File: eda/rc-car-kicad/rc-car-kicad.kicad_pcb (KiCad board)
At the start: 2 copper layers, 88.5 x 40.5 mm, 59 parts, among them J1 Servo Sig, J10 RF 3.3V, J11 RF CE, J12 RF CSN, J13 RF SCK, J14 RF MOSI, J15 RF MISO, J16 Gnd, J17 3.3V, J19 Battery, J2 Servo Gnd, J20 8.2V, J4 DC Motor -, J5 DC Motor +, J6 ISP RESET, J9 RF Gnd, Q1 IRLML6244, Q2 IRLML2246, Q3 IRLML2246, Q4 IRLML6244, Q5 MMBT3904, Q6 MMBT3904, SW1 SW_SPST, U1 TPS3840, U3 ATmega164A-A

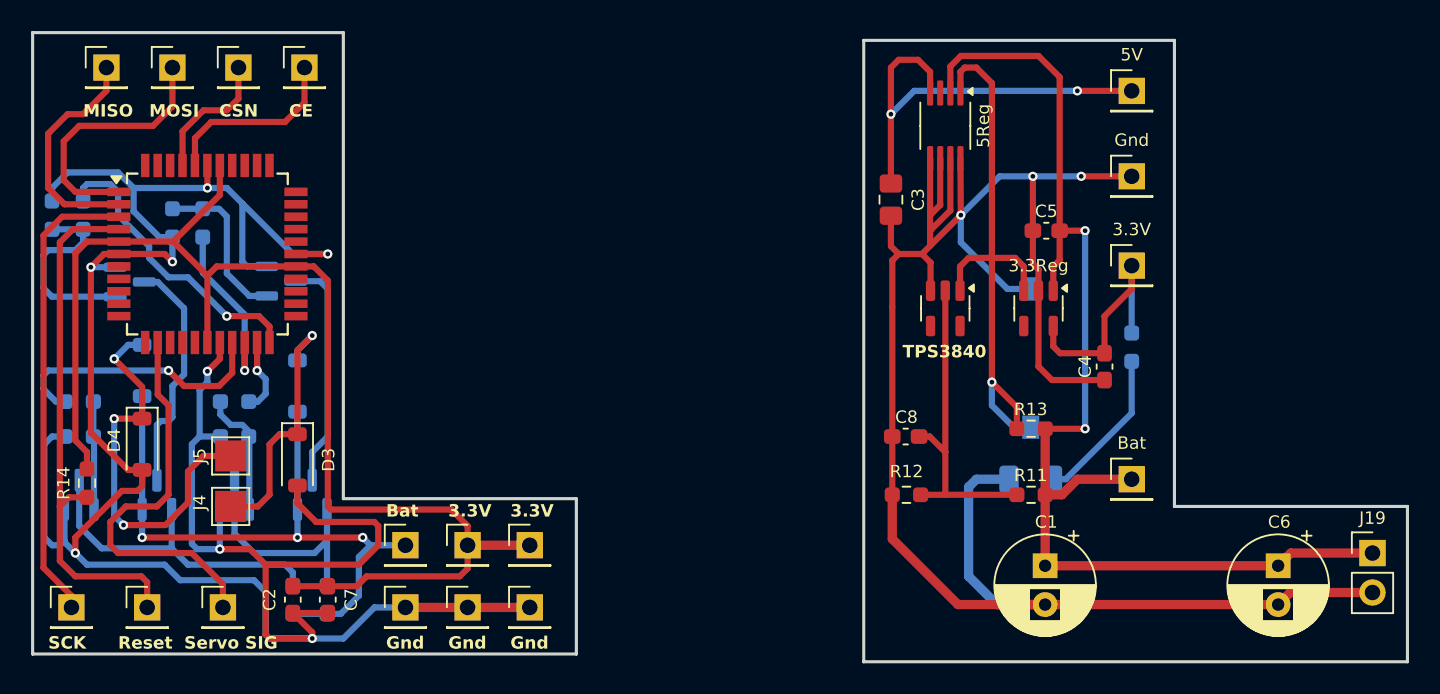
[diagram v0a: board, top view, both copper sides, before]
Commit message: - Redesigned power portion of the pcb - Changed the board to atmega164A
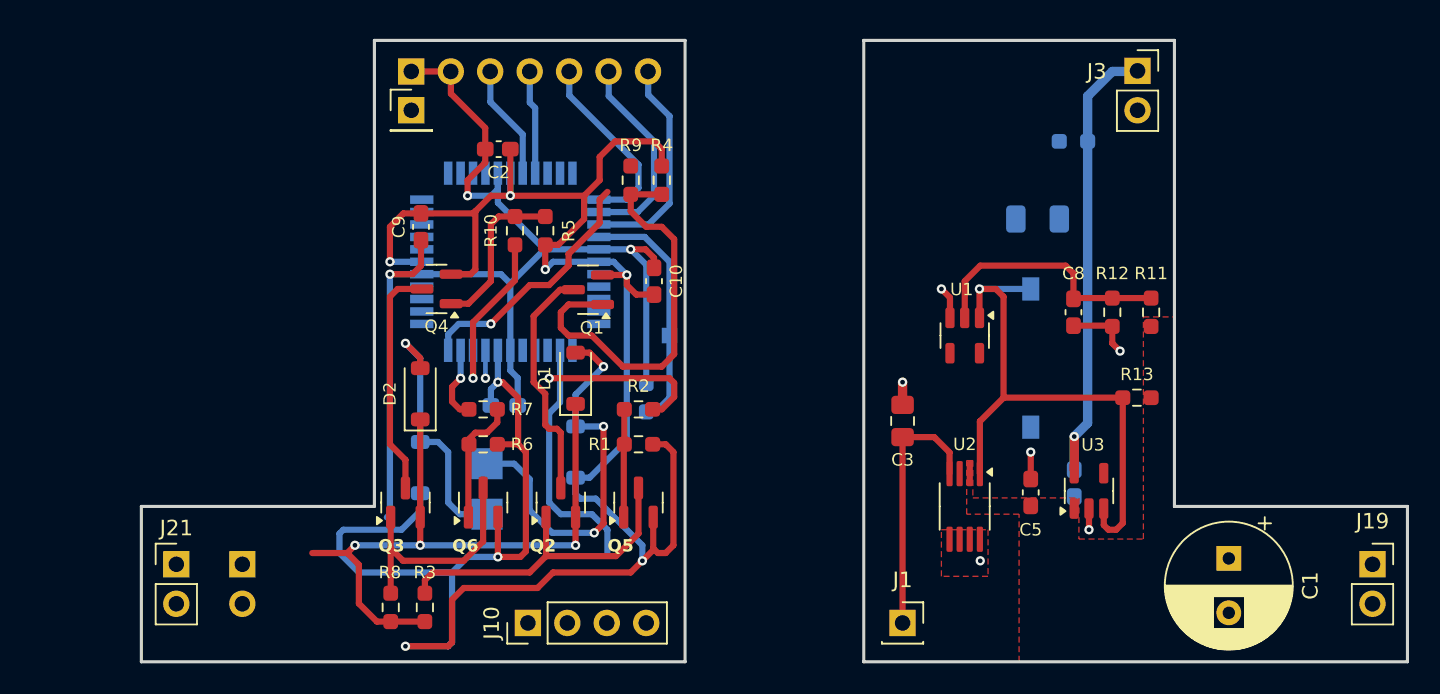
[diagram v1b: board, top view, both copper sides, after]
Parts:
- removed 3.3V, J17: 3.3V, Connector_PinHeader_2.54mm:PinHeader_1x01_P2.54mm_Vertical
- removed 5V: Servo 5V, Connector_PinHeader_2.54mm:PinHeader_1x01_P2.54mm_Vertical
- removed Bat, J20: 8.2V, Connector_PinHeader_2.54mm:PinHeader_1x01_P2.54mm_Vertical
- removed the C1 at (165.2, 134.3)
- removed Gnd: Gnd, Connector_PinHeader_2.54mm:PinHeader_1x01_P2.54mm_Vertical
- removed J12: RF CSN, Connector_PinHeader_2.54mm:PinHeader_1x01_P2.54mm_Vertical
- removed J13: RF SCK, Connector_PinHeader_2.54mm:PinHeader_1x01_P2.54mm_Vertical
- removed J14: RF MOSI, Connector_PinHeader_2.54mm:PinHeader_1x01_P2.54mm_Vertical
- removed J15: RF MISO, Connector_PinHeader_2.54mm:PinHeader_1x01_P2.54mm_Vertical
- removed J9: RF Gnd, Connector_PinHeader_2.54mm:PinHeader_1x01_P2.54mm_Vertical
- added C10: .1uF, Capacitor_SMD:C_0603_1608Metric_Pad1.08x0.95mm_HandSolder, F.Cu at (140.0, 116.0)
- added C9: .1uF, Capacitor_SMD:C_0603_1608Metric_Pad1.08x0.95mm_HandSolder, F.Cu at (125.0, 112.5)
- added J21: Battery, Connector_PinHeader_2.54mm:PinHeader_1x02_P2.54mm_Vertical, F.Cu at (109.2, 134.2)
- added J3: Battery, Connector_PinSocket_2.54mm:PinSocket_1x02_P2.54mm_Vertical, F.Cu at (171.1, 102.5)
- C1: renamed from C6; value 100uF -> 200uF; footprint Capacitor_THT:CP_Radial_D6.3mm_P2.50mm -> Capacitor_THT:CP_Radial_D8.0mm_P3.50mm
- C4, C7, D3, D4, J4, J5, R14: moved to B.Cu
- D1, D2, Q1, Q2, Q3, Q4, Q5, Q6, R1, R10, R2, R3, R4, R5, R6, R7, R8, R9: moved to F.Cu
- J1: value Servo Sig -> 5V; footprint Connector_PinHeader_2.54mm:PinHeader_1x01_P2.54mm_Vertical -> Connector_PinSocket_2.54mm:PinSocket_1x01_P2.54mm_Vertical
- J10: value RF 3.3V -> Conn_01x04; footprint Connector_PinHeader_2.54mm:PinHeader_1x01_P2.54mm_Vertical -> Connector_PinHeader_2.54mm:PinHeader_1x04_P2.54mm_Vertical
- J11: value RF CE -> Conn_01x07; footprint Connector_PinHeader_2.54mm:PinHeader_1x01_P2.54mm_Vertical -> Connector_PinHeader_2.54mm:PinHeader_1x07_P2.54mm_Vertical; moved to B.Cu
- J19: footprint Connector_PinHeader_2.54mm:PinHeader_1x02_P2.54mm_Vertical -> Connector_PinSocket_2.54mm:PinSocket_1x02_P2.54mm_Vertical
- J2: value Servo Gnd -> Battery; footprint Connector_PinHeader_2.54mm:PinHeader_1x01_P2.54mm_Vertical -> Connector_PinHeader_2.54mm:PinHeader_1x02_P2.54mm_Vertical; moved to B.Cu
- J6: footprint Connector_PinHeader_2.54mm:PinHeader_1x01_P2.54mm_Vertical -> TestPoint:TestPoint_Pad_1.0x1.0mm; moved to B.Cu
- R11: value 953k -> 470k
- R12: value 1M -> 500k
- U4: renamed from U3; moved to B.Cu
- moved J1 43.8 mm to (156.0, 138.0)
- moved R4 39.3 mm to (140.5, 109.5)
- moved J6 37.9 mm to (141.0, 119.5), turned to 180 degrees
- moved R14 36.4 mm to (139.5, 123.5)
- moved Q5 36.0 mm to (139.0, 130.2)
- moved R1 36.0 mm to (139.0, 126.5), turned to 0 degrees
- moved R2 36.0 mm to (139.0, 124.2), turned to 180 degrees
- moved R9 35.3 mm to (138.5, 109.5)
- moved J16 32.9 mm to (124.4, 105.0)
- moved C2 31.9 mm to (130.0, 107.5), turned to 0 degrees
- moved Q1 29.5 mm to (135.8, 116.5), turned to 180 degrees
- moved D1 27.9 mm to (134.9, 122.2)
- moved D4 27.9 mm to (134.9, 127.0)
- moved Q2 26.0 mm to (134.0, 130.2)
- moved U2 24.5 mm to (160.0, 130.5)
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- renumbered 5Reg to U2, 3.3Reg to U3
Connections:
- net Net-(SW1-B) renamed /U1-Reset
- net Net-(U1-VDD) renamed /U1-VDD
- C3 pad 1: +5V -> +5V Main
- J1 pad 1: /Servo Sig -> +5V Main
- J10 pad 1: +3.3V -> /Servo Sig
- J11 pad 1: /CE -> +3.3V
- J2 pad 1: GND -> +8.2V
- Q1 pad 3: Net-(Q1-D) -> Net-(D1-A)
- Q2 pad 3: Net-(Q1-D) -> Net-(D1-A)
- Q3 pad 3: Net-(Q3-D) -> Net-(D2-A)
- Q4 pad 3: Net-(Q3-D) -> Net-(D2-A)
- U2 pad 4: +5V -> +5V Main
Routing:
- net GND Main: track 130.9 -> 11.0 mm, vias 3 -> 6
- net +8.2V Main: track 76.7 -> 0.00 mm, vias 2 -> 0
- net +5V: track 28.0 -> 0.00 mm, vias 2 -> 0
- net /RESET: track 34.5 -> 15.8 mm
- net +3.3V Main: track 15.5 -> 32.8 mm, vias 0 -> 1
- net +5V Main: track 0.00 -> 16.8 mm
- net /SCK: track 30.0 -> 14.2 mm
- net Net-(D1-A): track 25.6 -> 40.9 mm
- net Net-(Q1-D): track 15.3 -> 0.00 mm
- net Net-(Q3-D): track 15.0 -> 0.00 mm
- net Net-(D2-A): track 16.9 -> 31.9 mm
- net Net-(Q1-G): track 12.7 -> 26.6 mm
- net Net-(D5-A): track 10.2 -> 0.00 mm
- net /Servo Sig: track 25.9 -> 16.1 mm
- net GND: track 163.5 -> 154.9 mm
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- added copper zone on F.Cu, net +8.2V Main
- added copper zone on B.Cu, net GND Main
- added copper zone on F.Cu, net GND Main
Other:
- board size 88.5 x 40.5 mm -> 81.5 x 40 mm
- board text added: "U1"
- board text added: "U3"
- board text removed: "Bat"
- board text removed: "Gnd"
- board text removed: "Reset"
- board text removed: "Servo SIG"
- board text removed: "TPS3840"

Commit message: - Made improvements to power and ground plains on the powere pcb - Updated the component labels in the schematic
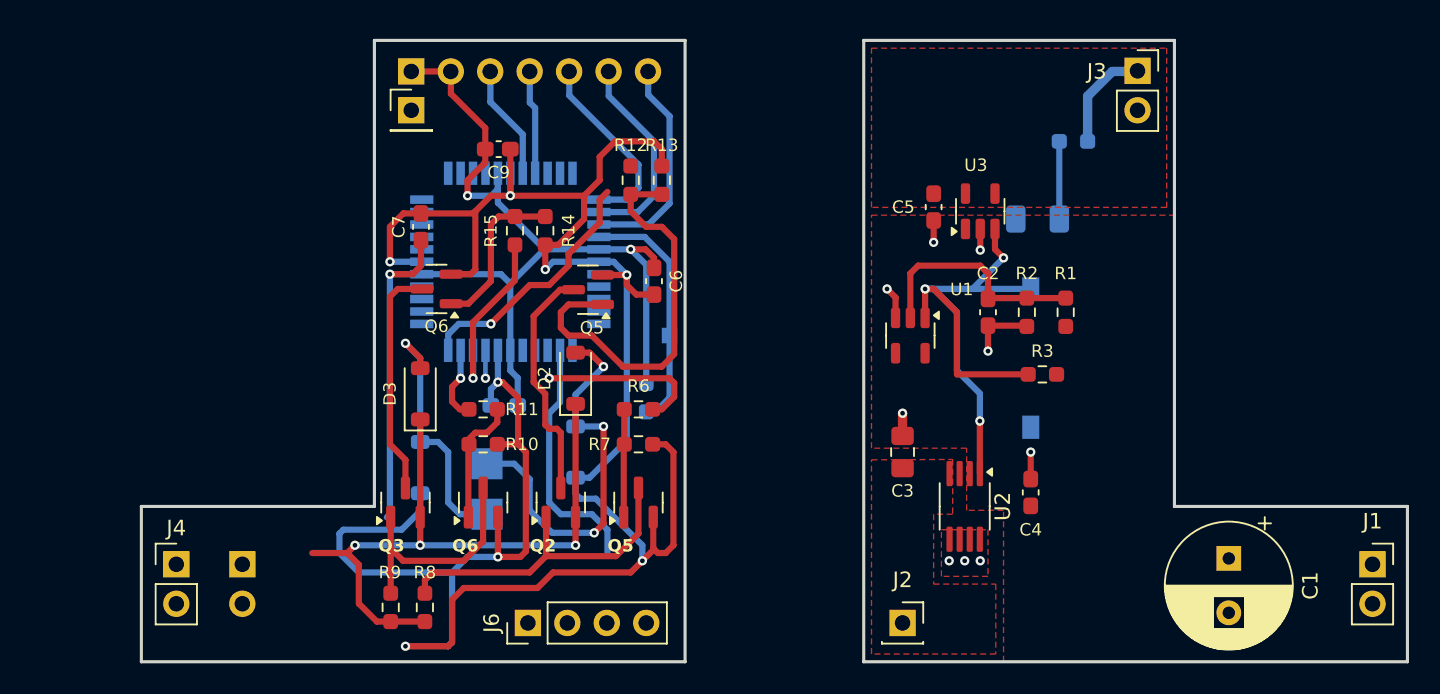
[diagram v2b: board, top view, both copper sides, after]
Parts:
- C5: renamed from C4; moved to F.Cu
- J1: renamed from J19; value Battery -> ~
- J10: renamed from J4; value DC Motor - -> ~
- J11: renamed from J6; value ISP RESET -> ~
- J2: renamed from J1; value 5V -> ~
- J3: value Battery -> ~
- J4: renamed from J21; value Battery -> ~
- J5: renamed from J2; value Battery -> ~
- J6: renamed from J10; value Conn_01x04 -> ~
- J7: renamed from J16; value Gnd -> ~
- J8: renamed from J11; value Conn_01x07 -> ~
- J9: renamed from J5; value DC Motor + -> ~
- moved C5 19.9 mm to (158.0, 111.2)
- moved U3 19.3 mm to (161.0, 111.5)
- moved R3 6.27 mm to (165.0, 122.0)
- moved C2 5.50 mm to (161.5, 118.0)
- moved R1 5.50 mm to (166.5, 118.0)
- moved R2 5.50 mm to (164.0, 118.0)
- moved U1 3.50 mm to (156.5, 119.5)
- moved C3 2.00 mm to (156.0, 127.0)
- renumbered C8 to C2, C5 to C4, C10 to C6, C9 to C7, C7 to C8, C2 to C9, D5 to D1, D1 to D2, D2 to D3, D3 to D5, Q5 to Q1, Q6 to Q4, Q1 to Q5, Q4 to Q6, R11 to R1, R6 to R10, R7 to R11, R9 to R12, R4 to R13, R5 to R14, R10 to R15, R12 to R2, R13 to R3, R15 to R4, R14 to R5, R2 to R6, R1 to R7, R3 to R8, R8 to R9
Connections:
- D1 pad 2: Net-(D5-A) -> Net-(D1-A)
- R4 pad 1: +3.3V Main -> Net-(D1-A)
- R4 pad 2: Net-(D5-A) -> +3.3V Main
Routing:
- net +3.3V Main: track 32.8 -> 6.78 mm, vias 1 -> 0
- net +5V Main: track 16.8 -> 0.00 mm
- net (no net): track 0.00 -> 5.00 mm
- net /U1-Reset: track 37.3 -> 41.6 mm, vias 1 -> 3
- net /U1-VDD: track 16.6 -> 14.9 mm
- net GND Main: track 11.0 -> 12.1 mm, vias 6 -> 9
- added copper zone on F.Cu, net +3.3V Main
- added copper zone on F.Cu, net +5V Main

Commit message: - Updated the microcontroller pcb
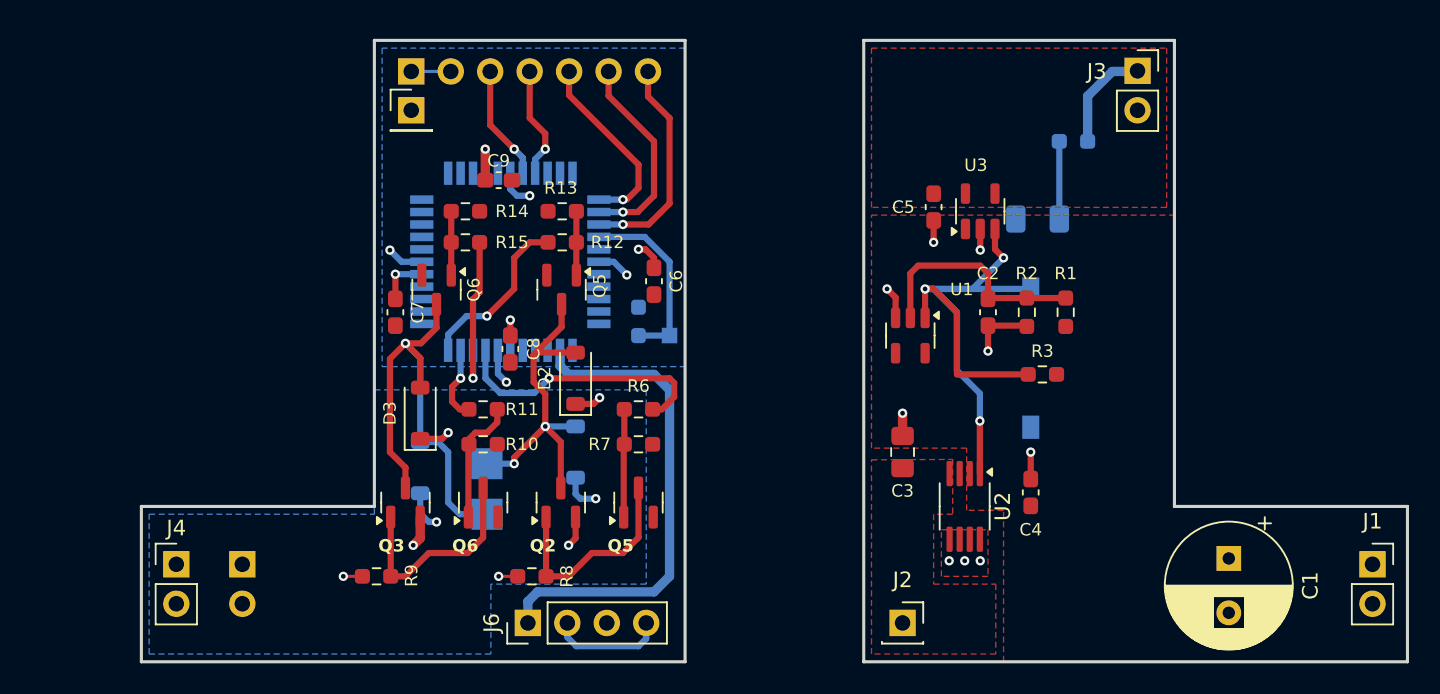
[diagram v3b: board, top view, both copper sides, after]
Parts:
- C8: moved to F.Cu
- moved R8 7.17 mm to (132.1, 135.0), turned to 0 degrees
- moved R13 6.71 mm to (134.1, 111.5), turned to 180 degrees
- moved R12 5.95 mm to (134.1, 113.5), turned to 0 degrees
- moved C7 5.74 mm to (123.3, 118.0), turned to -90 degrees
- moved R14 5.29 mm to (127.9, 111.5), turned to 0 degrees
- moved R5 4.94 mm to (139.0, 118.6)
- moved C8 3.66 mm to (130.8, 120.4), turned to -90 degrees
- moved R15 3.28 mm to (127.9, 113.5), turned to 0 degrees
- moved R9 2.20 mm to (122.1, 135.0), turned to 0 degrees
- moved C9 2.00 mm to (130.0, 109.5)
- moved Q5 1.70 mm to (134.1, 116.5), turned to -90 degrees
- moved D3 1.25 mm to (125.0, 124.5)
- turned Q6 to -90 degrees
- turned R4 to 0 degrees
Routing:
- net GND: track 154.9 -> 14.3 mm, vias 8 -> 6
- net +3.3V: track 76.9 -> 10.7 mm, vias 3 -> 4
- net +8.2V: track 42.6 -> 10.1 mm, vias 3 -> 6
- net Net-(Q5-G): track 26.6 -> 4.11 mm
- net Net-(D2-A): track 40.9 -> 23.0 mm, vias 3 -> 2
- net /Servo Sig: track 16.1 -> 31.9 mm
- net /Servo 5V: track 0.00 -> 7.45 mm
- net Net-(Q1-C): track 21.3 -> 14.0 mm
- net Net-(Q6-G): track 10.5 -> 4.11 mm
- net /Reverse_PWM: track 16.4 -> 11.1 mm
- net Net-(D1-A): track 0.00 -> 5.00 mm
- net (no net): track 5.00 -> 0.00 mm
- net /Forward_Latch: track 12.6 -> 17.5 mm, vias 2 -> 1
- net /RESET: track 15.8 -> 12.0 mm
- net Net-(Q3-G): track 15.1 -> 14.0 mm
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- added copper zone on B.Cu, net +3.3V
- added copper zone on B.Cu, net +8.2V
- added copper zone on F.Cu, net GND

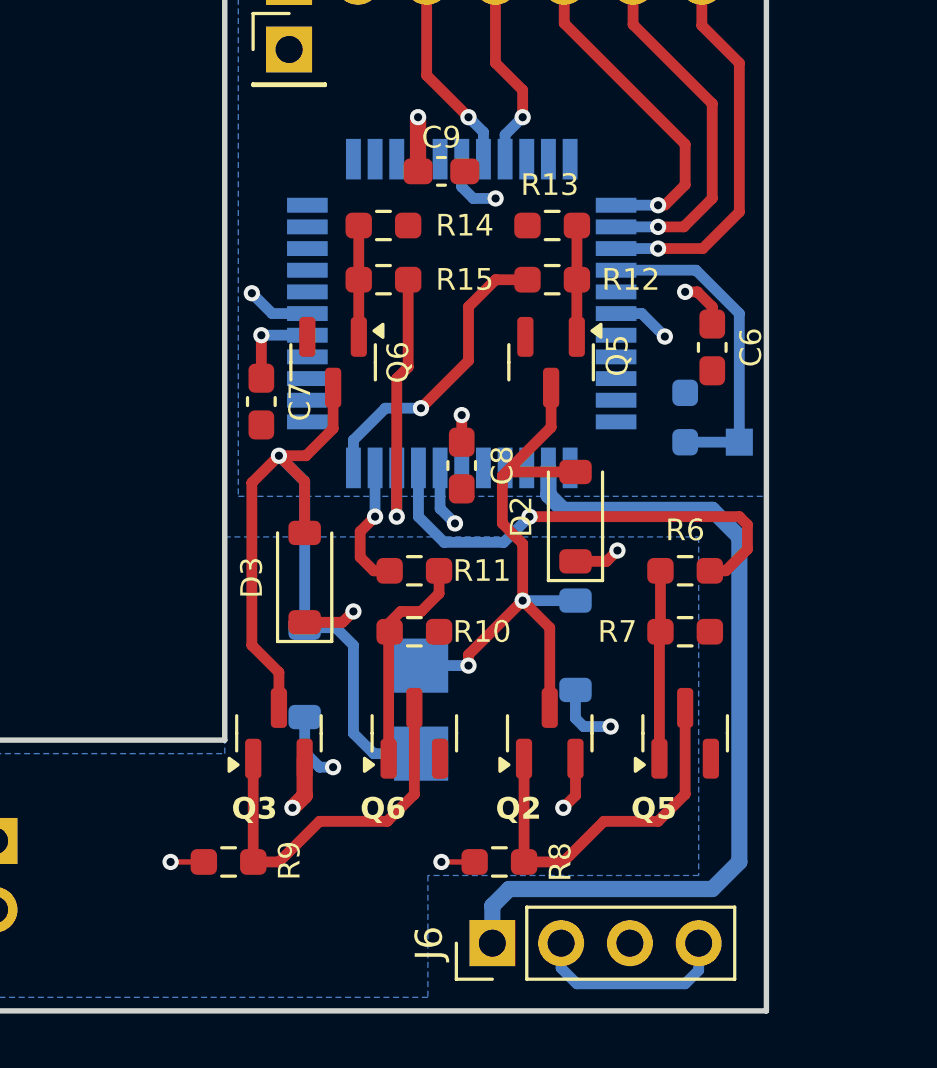
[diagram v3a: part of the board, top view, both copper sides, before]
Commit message: - Added testing points for H-Bridge connections to the PCB
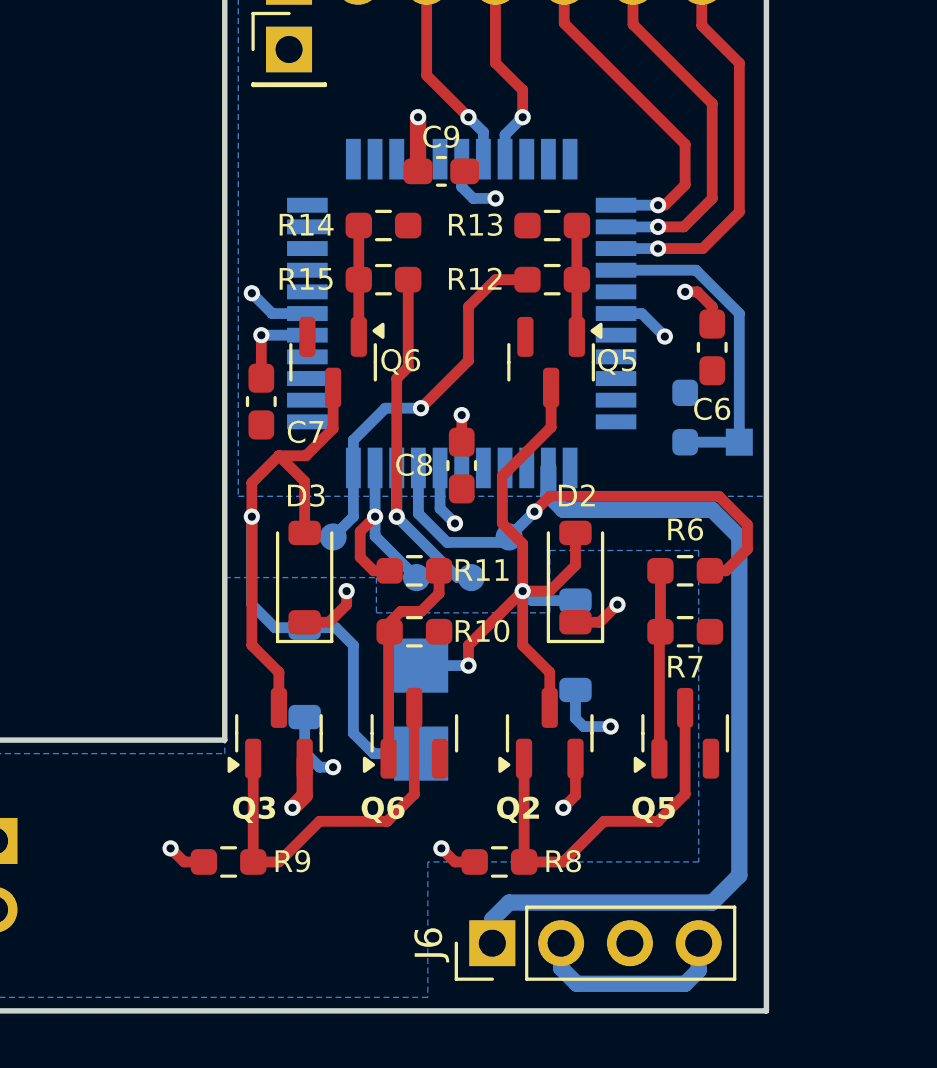
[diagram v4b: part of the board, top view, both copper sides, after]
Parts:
- added J12: ~, TestPoint:TestPoint_Pad_D1.0mm, B.Cu at (132.5, 123.0)
- added J13: ~, TestPoint:TestPoint_Pad_D1.0mm, B.Cu at (131.1, 124.5)
- added J14: ~, TestPoint:TestPoint_Pad_D1.0mm, B.Cu at (129.1, 124.5)
- added J15: ~, TestPoint:TestPoint_Pad_D1.0mm, B.Cu at (126.0, 123.0)
- moved D2 2.25 mm to (134.9, 124.5)
- renumbered J9 to Motor+, J10 to Motor-
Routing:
- net /Forward_PWM: track 10.7 -> 14.4 mm
- net /Reverse_Latch: track 4.87 -> 7.75 mm
- net /Reverse_PWM: track 11.1 -> 13.9 mm
- net Net-(D2-A): track 23.0 -> 24.3 mm
- net Net-(D3-A): track 32.2 -> 31.0 mm
- net +8.2V: track 10.1 -> 11.0 mm
- net /Forward_Latch: track 17.5 -> 18.0 mm
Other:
- board text added: "Gnd"
